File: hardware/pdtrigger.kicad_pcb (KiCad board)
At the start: 4 copper layers, 56 x 53 mm, 93 parts, among them J1 Conn_01x04_Pin, J2 USB_C_Receptacle_USB2.0_16P, J3 Conn_01x02_Pin, Q1 DMP3098LSD-13, Q3 NMOS, SW1 SW_SPDT, SW2 SW_Push, U1 STM32F401RBT6, U2 CYPD3177-24LQXQ, U3 TERM_BLK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

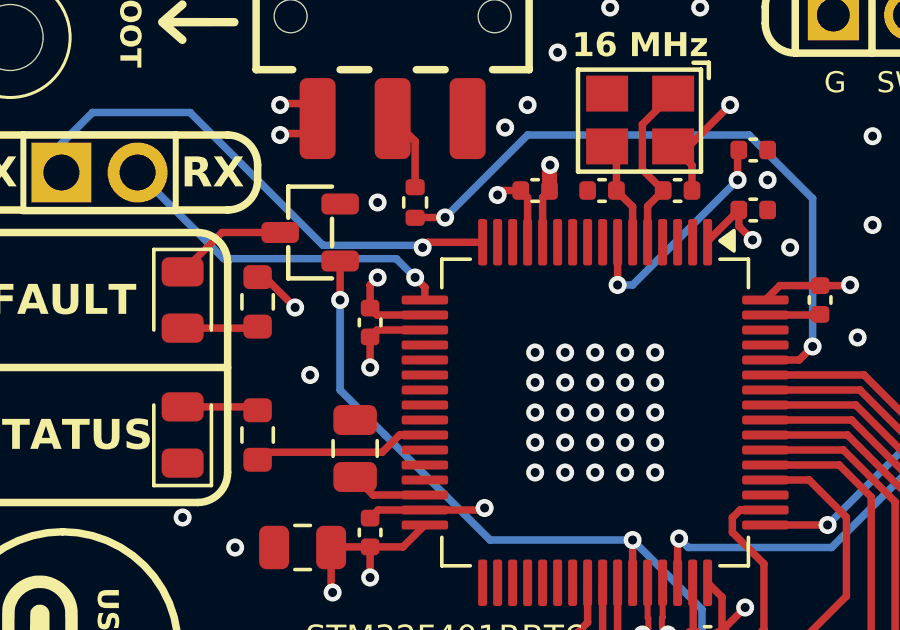
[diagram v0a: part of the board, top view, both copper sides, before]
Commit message: firmware work after finally debugging hardware
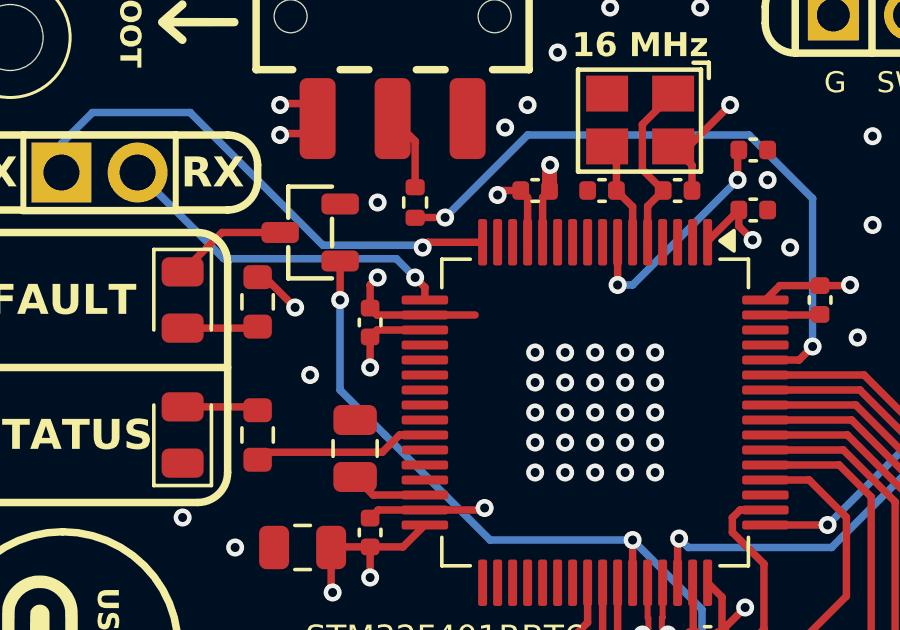
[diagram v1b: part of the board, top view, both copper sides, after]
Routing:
- net GND: track 38.6 -> 40.2 mm
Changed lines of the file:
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@@
+	)
+	(segment
+		(start 142.825 101.75)
+		(end 144.5 101.75)
+		(width 0.25)
+		(layer "F.Cu")
+		(net 1)
 	)
 	(segment
